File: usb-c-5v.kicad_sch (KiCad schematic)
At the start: 10 parts, among them J6 USB_C_Receptacle, U8 AP2112K-3.3

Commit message: Started running traces
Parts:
- C30, C31: footprint (none) -> Capacitor_SMD:C_0805_2012Metric
- C32: footprint (none) -> Capacitor_SMD:C_0603_1608Metric
- J6: value USB_C_Receptacle -> KH-TYPE-C-16P (Kinghelm); footprint (none) -> Connector_USB:USB_C_Receptacle_GCT_USB4110
- R3, R4, R5, R6: footprint (none) -> Resistor_SMD:R_0402_1005Metric
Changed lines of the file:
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@@
 			)
 		)
-		(property "Footprint" ""
+		(property "Footprint" "Resistor_SMD:R_0402_1005Metric"
 			(at 77.47 42.418 90)
 			(effects
@@
 			)
 		)
-		(property "Footprint" ""
+		(property "Footprint" "Capacitor_SMD:C_0805_2012Metric"
 			(at 133.0452 59.69 0)
 			(effects
@@
 			)
 		)
-		(property "Footprint" ""
+		(property "Footprint" "Resistor_SMD:R_0402_1005Metric"
 			(at 73.66 52.578 90)
 			(effects
@@
 			)
 		)
-		(property "Value" "USB_C_Receptacle"
+		(property "Value" "KH-TYPE-C-16P (Kinghelm)"
 			(at 40.64 21.59 0)
 			(effects
@@
 			)
 		)
-		(property "Footprint" ""
+		(property "Footprint" "Connector_USB:USB_C_Receptacle_GCT_USB4110"
 			(at 44.45 52.07 0)
 			(effects
@@
 			)
 		)
-		(property "Footprint" ""
+		(property "Footprint" "Resistor_SMD:R_0402_1005Metric"
 			(at 69.85 29.972 90)
 			(effects
@@
 			)
 		)
-		(property "Footprint" ""
+		(property "Footprint" "Capacitor_SMD:C_0805_2012Metric"
 			(at 108.9152 59.69 0)
 			(effects
@@
 			)
 		)
-		(property "Footprint" ""
+		(property "Footprint" "Capacitor_SMD:C_0603_1608Metric"
 			(at 144.4752 59.69 0)
 			(effects
@@
 			)
 		)
-		(property "Footprint" ""
+		(property "Footprint" "Resistor_SMD:R_0402_1005Metric"
 			(at 59.69 32.512 90)
 			(effects

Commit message: Finishing touches
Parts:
- J6: footprint Connector_USB:USB_C_Receptacle_GCT_USB4110 -> KH-TYPE-C-16P:KINGHELM_KH-TYPE-C-16P; symbol Connector:USB_C_Receptacle -> KH-TYPE-C-16P:KH-TYPE-C-16P; Availability (none) -> Not in stock; Check_prices (none) -> https://www.snapeda.com/parts/KH-TYPE-C-16P/Kinghelm/view-p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; MANUFACTURER (none) -> Kinghelm; MAXIMUM_PACKAGE_HEIGHT (none) -> 3.41mm; MF (none) -> kinghelm; MP (none) -> KH-TYPE-C-16P; PARTREV (none) -> A0; Package (none) -> None; Price (none) -> None; SNAPEDA_PN (none) -> KH-TYPE-C-16P; STANDARD (none) -> Manufacturer Recommendations; SnapEDA_Link (none) -> https://www.snapeda.com/parts/KH-TYPE-C-16P/Kinghelm/view-p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
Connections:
- net DN: now reaches J6.A7 (DN1), J6.B7 (DN2)
- net DN: now also R4.1; no longer R3.1
- net DP: now reaches J6.A6 (DP1), J6.B6 (DP2)
- net DP: now also R3.1; no longer R4.1
- net GND_ISO renamed GND
- net GND: now also J6.A12_B1 (GND), J6.A1_B12 (GND), J6.SH1 (SHIELD), J6.SH2 (SHIELD), J6.SH3 (SHIELD), J6.SH4 (SHIELD); no longer J6.A1 (GND), J6.A12 (GND), J6.B1 (GND), J6.B12 (GND), J6.S1 (SHIELD)
- new net VBUS: D2.1 (A), J6.A4_B9 (VBUS), J6.A9_B4 (VBUS)
- no-connect marks 10 -> 2
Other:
- moved on the sheet: R3, R4, R5, R6

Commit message: BOM work
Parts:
- C4: renamed from C30; value 10uF -> 10uF 10V; LCSC (none) -> C17024
- C5: renamed from C31; LCSC (none) -> C5674
- C6: renamed from C32; LCSC (none) -> C1590
- D2: LCSC (none) -> C8592
- J2: renamed from J6; LCSC (none) -> C709357
- R1: renamed from R5; LCSC (none) -> C25905
- R2: renamed from R4; LCSC (none) -> C25092
- R3: LCSC (none) -> C25092
- R4: renamed from R6; LCSC (none) -> C25905
- U2: renamed from U8; LCSC (none) -> C23380830
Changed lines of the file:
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@@
 		(dnp no)
 		(fields_autoplaced yes)
-		(property "Reference" "#PWR042"
+		(property "Reference" "#PWR015"
 			(at 146.05 52.07 0)
 			(effects
@@
 			(project "barn-blinds-controller"
 				(path "/aa90962a-81b9-423d-8acd-c4e83fa798bb/52efa7a4-2a50-492f-ba41-4a5be1c27b4c"
-					(reference "#PWR042")
+					(reference "#PWR015")
 					(unit 1)
 				)
@@
 		(dnp no)
 		(fields_autoplaced yes)
-		(property "Reference" "#PWR040"
+		(property "Reference" "#PWR09"
 			(at 101.6 50.8 0)
 			(effects
@@
 			(project "barn-blinds-controller"
 				(path "/aa90962a-81b9-423d-8acd-c4e83fa798bb/52efa7a4-2a50-492f-ba41-4a5be1c27b4c"
-					(reference "#PWR040")
+					(reference "#PWR09")
 					(unit 1)
 				)
@@
 			)
 		)
+		(property "LCSC" "C25092"
+			(at 69.85 76.2 90)
+			(effects
+				(font
+					(size 1.27 1.27)
+				)
+				(hide yes)
+			)
+		)
 		(pin "1"
 		)
@@
 		(dnp no)
 		(fields_autoplaced yes)
-		(property "Reference" "C31"
+		(property "Reference" "C5"
 			(at 135.89 53.7209 0)
 			(effects
@@
 			)
 		)
+		(property "LCSC" "C5674"
+			(at 132.08 55.88 0)
+			(effects
+				(font
+					(size 1.27 1.27)
+				)
+				(hide yes)
+			)
+		)
 		(pin "2"
 		)
@@
 			(project "barn-blinds-controller"
 				(path "/aa90962a-81b9-423d-8acd-c4e83fa798bb/52efa7a4-2a50-492f-ba41-4a5be1c27b4c"
-					(reference "C31")
+					(reference "C5")
 					(unit 1)
 				)
@@
 		(dnp no)
 		(fields_autoplaced yes)
-		(property "Reference" "#PWR038"
+		(property "Reference" "#PWR06"
 			(at 36.83 55.88 0)
 			(effects
@@
 			(project "barn-blinds-controller"
 				(path "/aa90962a-81b9-423d-8acd-c4e83fa798bb/52efa7a4-2a50-492f-ba41-4a5be1c27b4c"
-					(reference "#PWR038")
+					(reference "#PWR06")
 					(unit 1)
 				)
@@
 		(dnp no)
 		(fields_autoplaced yes)
-		(property "Reference" "#PWR043"
+		(property "Reference" "#PWR012"
 			(at 121.92 68.58 0)
 			(effects
@@
 			(project "barn-blinds-controller"
 				(path "/aa90962a-81b9-423d-8acd-c4e83fa798bb/52efa7a4-2a50-492f-ba41-4a5be1c27b4c"
-					(reference "#PWR043")
+					(reference "#PWR012")
 					(unit 1)
 				)
@@
 		(on_board yes)
 		(dnp no)
-		(property "Reference" "R4"
+		(property "Reference" "R2"
 			(at 69.85 67.056 90)
 			(effects
@@
 			)
 		)
+		(property "LCSC" "C25092"
+			(at 69.85 67.31 90)
+			(effects
+				(font
+					(size 1.27 1.27)
+				)
+				(hide yes)
+			)
+		)
 		(pin "1"
 		)
@@
 			(project "barn-blinds-controller"
 				(path "/aa90962a-81b9-423d-8acd-c4e83fa798bb/52efa7a4-2a50-492f-ba41-4a5be1c27b4c"
-					(reference "R4")
+					(reference "R2")
 					(unit 1)
 				)
@@
 		(dnp no)
 		(fields_autoplaced yes)
-		(property "Reference" "J6"
+		(property "Reference" "J2"
 			(at 54.61 21.59 0)
 			(effects
@@
 			)
 		)
+		(property "LCSC" "C709357"
+			(at 54.61 36.83 0)
+			(effects
+				(font
+					(size 1.27 1.27)
+				)
+				(hide yes)
+			)
+		)
 		(pin "B5"
 		)
@@
 			(project "barn-blinds-controller"
 				(path "/aa90962a-81b9-423d-8acd-c4e83fa798bb/52efa7a4-2a50-492f-ba41-4a5be1c27b4c"
-					(reference "J6")
+					(reference "J2")
 					(unit 1)
 				)
@@
 			)
 		)
+		(property "LCSC" "C8592"
+			(at 101.6 40.64 0)
+			(effects
+				(font
+					(size 1.27 1.27)
+				)
+				(hide yes)
+			)
+		)
 		(pin "1"
 		)
@@
 		(on_board yes)
 		(dnp no)
-		(property "Reference" "#PWR037"
+		(property "Reference" "#PWR08"
 			(at 87.63 41.91 0)
 			(effects
@@
 			(project "barn-blinds-controller"
 				(path "/aa90962a-81b9-423d-8acd-c4e83fa798bb/52efa7a4-2a50-492f-ba41-4a5be1c27b4c"
-					(reference "#PWR037")
+					(reference "#PWR08")
 					(unit 1)
 				)
@@
 		(dnp no)
 		(fields_autoplaced yes)
-		(property "Reference" "#PWR045"
+		(property "Reference" "#PWR013"
 			(at 132.08 66.04 0)
 			(effects
@@
 			(project "barn-blinds-controller"
 				(path "/aa90962a-81b9-423d-8acd-c4e83fa798bb/52efa7a4-2a50-492f-ba41-4a5be1c27b4c"
-					(reference "#PWR045")
+					(reference "#PWR013")
 					(unit 1)
 				)
@@
 		(dnp no)
 		(fields_autoplaced yes)
-		(property "Reference" "#PWR034"
+		(property "Reference" "#PWR05"
 			(at 20.32 34.29 0)
 			(effects
@@
 			(project "barn-blinds-controller"
 				(path "/aa90962a-81b9-423d-8acd-c4e83fa798bb/52efa7a4-2a50-492f-ba41-4a5be1c27b4c"
-					(reference "#PWR034")
+					(reference "#PWR05")
 					(unit 1)
 				)
@@
 		(on_board yes)
 		(dnp no)
-		(property "Reference" "R5"
+		(property "Reference" "R1"
 			(at 32.766 34.036 90)
 			(effects
@@
 			)
 		)
+		(property "LCSC" "C25905"
+			(at 33.02 34.29 90)
+			(effects
+				(font
+					(size 1.27 1.27)
+				)
+				(hide yes)
+			)
+		)
 		(pin "2"
 		)
@@
 			(project "barn-blinds-controller"
 				(path "/aa90962a-81b9-423d-8acd-c4e83fa798bb/52efa7a4-2a50-492f-ba41-4a5be1c27b4c"
-					(reference "R5")
+					(reference "R1")
 					(unit 1)
 				)
@@
 		(dnp no)
 		(fields_autoplaced yes)
-		(property "Reference" "#PWR044"
+		(property "Reference" "#PWR010"
 			(at 107.95 66.04 0)
 			(effects
@@
 			(project "barn-blinds-controller"
 				(path "/aa90962a-81b9-423d-8acd-c4e83fa798bb/52efa7a4-2a50-492f-ba41-4a5be1c27b4c"
-					(reference "#PWR044")
+					(reference "#PWR010")
 					(unit 1)
 				)
@@
 		(on_board yes)
 		(dnp no)
-		(fields_autoplaced yes)
-		(property "Reference" "C30"
-			(at 111.76 53.7209 0)
+		(property "Reference" "C4"
+			(at 109.982 54.864 0)
 			(effects
 				(font
@@
 			)
 		)
-		(property "Value" "10uF"
-			(at 111.76 56.2609 0)
+		(property "Value" "10uF 10V"
+			(at 109.728 57.912 0)
 			(effects
 				(font
@@
 			)
 		)
+		(property "LCSC" "C17024"
+			(at 107.95 55.88 0)
+			(effects
+				(font
+					(size 1.27 1.27)
+				)
+				(hide yes)
+			)
+		)
 		(pin "2"
 		)
@@
 			(project "barn-blinds-controller"
 				(path "/aa90962a-81b9-423d-8acd-c4e83fa798bb/52efa7a4-2a50-492f-ba41-4a5be1c27b4c"
-					(reference "C30")
+					(reference "C4")
 					(unit 1)
 				)
@@
 		(dnp no)
 		(fields_autoplaced yes)
-		(property "Reference" "U8"
+		(property "Reference" "U2"
 			(at 121.92 45.72 0)
 			(effects
@@
 			)
 		)
+		(property "LCSC" "C23380830"
+			(at 121.92 54.61 0)
+			(effects
+				(font
+					(size 1.27 1.27)
+				)
+				(hide yes)
+			)
+		)
 		(pin "4"
 		)
@@
 			(project "barn-blinds-controller"
 				(path "/aa90962a-81b9-423d-8acd-c4e83fa798bb/52efa7a4-2a50-492f-ba41-4a5be1c27b4c"
-					(reference "U8")
+					(reference "U2")
 					(unit 1)
 				)
@@
 		(dnp no)
 		(fields_autoplaced yes)
-		(property "Reference" "C32"
+		(property "Reference" "C6"
 			(at 147.32 54.6099 0)
 			(effects
@@
 			)
 		)
+		(property "LCSC" "C1590"
+			(at 143.51 55.88 0)
+			(effects
+				(font
+					(size 1.27 1.27)
+				)
+				(hide yes)
+			)
+		)
 		(pin "1"
 		)
@@
 			(project "barn-blinds-controller"
 				(path "/aa90962a-81b9-423d-8acd-c4e83fa798bb/52efa7a4-2a50-492f-ba41-4a5be1c27b4c"
-					(reference "C32")
+					(reference "C6")
 					(unit 1)
 				)
@@
 		(dnp no)
 		(fields_autoplaced yes)
-		(property "Reference" "#PWR046"
+		(property "Reference" "#PWR014"
 			(at 143.51 66.04 0)
 			(effects
@@
 			(project "barn-blinds-controller"
 				(path "/aa90962a-81b9-423d-8acd-c4e83fa798bb/52efa7a4-2a50-492f-ba41-4a5be1c27b4c"
-					(reference "#PWR046")
+					(reference "#PWR014")
 					(unit 1)
 				)
@@
 		(on_board yes)
 		(dnp no)
-		(property "Reference" "#PWR039"
+		(property "Reference" "#PWR011"
 			(at 107.95 40.64 0)
 			(effects
@@
 			(project "barn-blinds-controller"
 				(path "/aa90962a-81b9-423d-8acd-c4e83fa798bb/52efa7a4-2a50-492f-ba41-4a5be1c27b4c"
-					(reference "#PWR039")
+					(reference "#PWR011")
 					(unit 1)
 				)
@@
 		(on_board yes)
 		(dnp no)
-		(property "Reference" "R6"
+		(property "Reference" "R4"
 			(at 76.454 41.91 90)
 			(effects
@@
 			)
 		)
+		(property "LCSC" "C25905"
+			(at 76.2 41.91 90)
+			(effects
+				(font
+					(size 1.27 1.27)
+				)
+				(hide yes)
+			)
+		)
 		(pin "1"
 		)
@@
 			(project "barn-blinds-controller"
 				(path "/aa90962a-81b9-423d-8acd-c4e83fa798bb/52efa7a4-2a50-492f-ba41-4a5be1c27b4c"
-					(reference "R6")
+					(reference "R4")
 					(unit 1)
 				)
@@
 		(on_board yes)
 		(dnp no)
-		(property "Reference" "#PWR033"
+		(property "Reference" "#PWR07"
 			(at 72.39 55.88 0)
 			(effects
@@
 			(project "barn-blinds-controller"
 				(path "/aa90962a-81b9-423d-8acd-c4e83fa798bb/52efa7a4-2a50-492f-ba41-4a5be1c27b4c"
-					(reference "#PWR033")
-					(unit 1)
-				)
+					(reference "#PWR07")
+					(unit 1)
+				)

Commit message: BOM work
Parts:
- J2: footprint KH-TYPE-C-16P:KINGHELM_KH-TYPE-C-16P -> barn_shade_controller:KINGHELM_KH-TYPE-C-16P
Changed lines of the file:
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@@
 			)
 		)
-		(property "Footprint" "KH-TYPE-C-16P:KINGHELM_KH-TYPE-C-16P"
+		(property "Footprint" "barn_shade_controller:KINGHELM_KH-TYPE-C-16P"
 			(at 54.61 36.83 0)
 			(effects

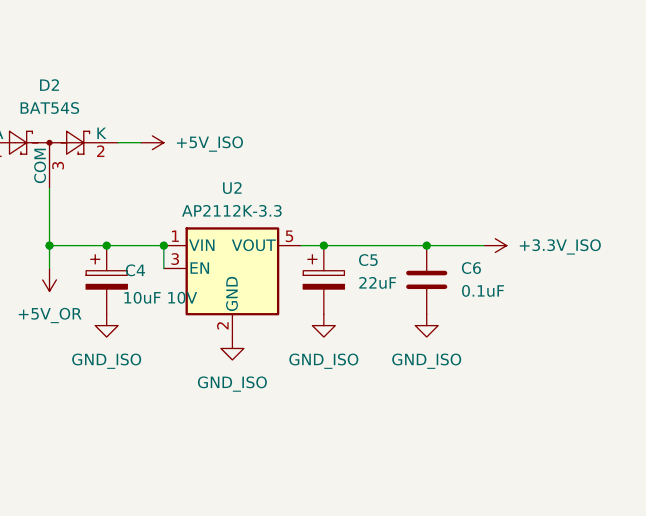
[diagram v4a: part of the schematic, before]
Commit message: Updated BOM, fixed a few components
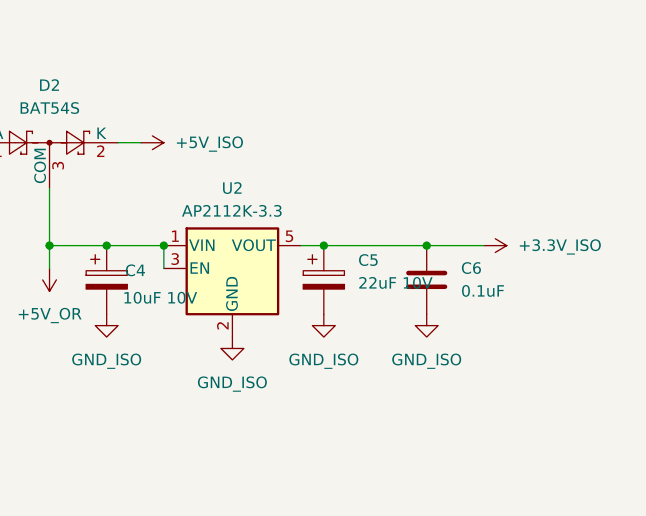
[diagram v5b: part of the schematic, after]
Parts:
- C5: value 22uF -> 22uF 10V; LCSC C5674 -> C29277
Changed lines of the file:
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@@
 			)
 		)
-		(property "Value" "22uF"
+		(property "Value" "22uF 10V"
 			(at 135.89 56.2609 0)
 			(effects
@@
 			)
 		)
-		(property "LCSC" "C5674"
+		(property "LCSC" "C29277"
 			(at 132.08 55.88 0)
 			(effects

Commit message: V 1.2
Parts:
- added TP1: 3.3V_ISO, barn_shade_controller:TestPoint_Pad_D1.0mm_No_SolderMask, symbol Connector:TestPoint
- D2: value BAT54S -> BAT54C; LCSC C8592 -> C2135
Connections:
- net +3.3V_ISO: now also TP1.1
- net GPIO19 renamed USB_DP
- net GPIO20 renamed USB_DN
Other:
- moved on the sheet: C5, C6, R1
